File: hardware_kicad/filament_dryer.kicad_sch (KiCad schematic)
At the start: 140 parts, among them J1 USB_C_Receptacle_USB2.0, J2 H/T Ambient, J3 T Aux, J4 Peristaltic Pump, Q3 NMOS, Q4 NMOS, Q5 NMOS, Q6 NMOS, Q7 NMOS, Q8 NMOS, U1 W25Q128JVS, U2 AMS1117-3.3, U3 RP2040, U4 DS18B20Z, U5 H/T Filament, X1 12MHz Yangxing Tech X322512MS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

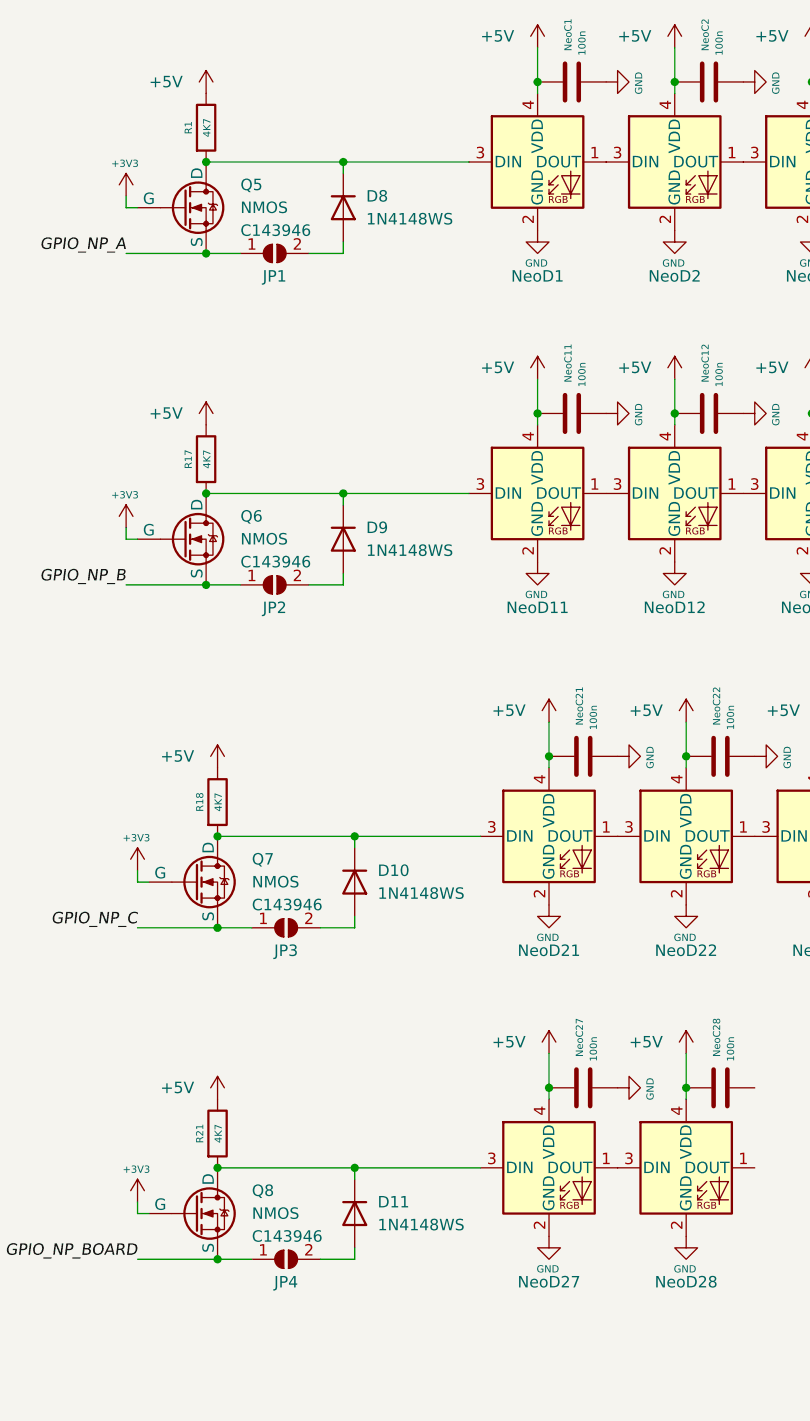
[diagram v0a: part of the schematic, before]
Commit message: Remove 4 diodes
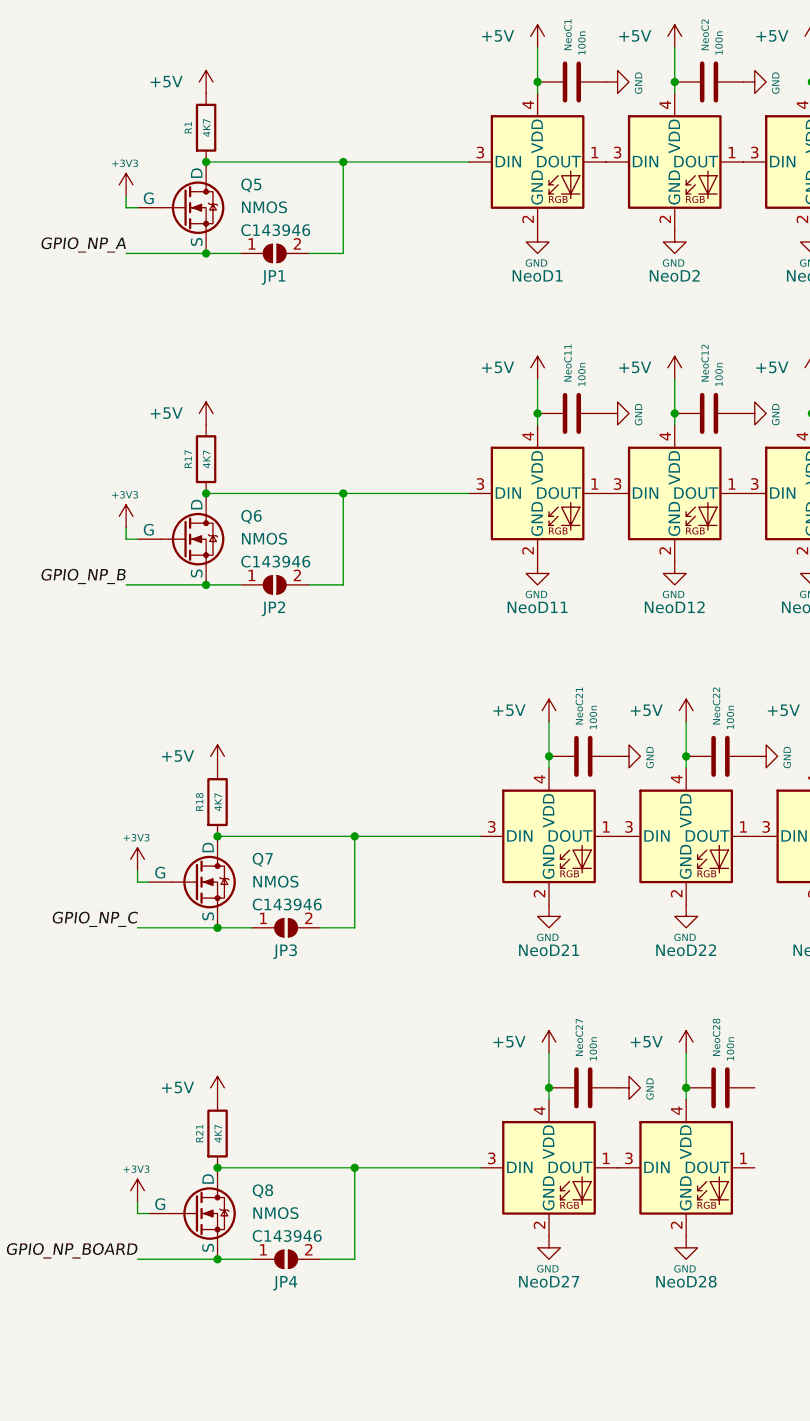
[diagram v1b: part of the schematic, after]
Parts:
- removed D10, D11, D8, D9: 1N4148WS, Diode_SMD:D_SOD-323, symbol Diode:1N4148WS
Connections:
- net at NeoD27.3 (DIN), Q8.1 (D), R21.2: now also JP4.2 (B)
- net at NeoD11.3 (DIN), Q6.1 (D), R17.2: now also JP2.2 (B)
- net at JP1.2 (B): now also NeoD1.3 (DIN), Q5.1 (D), R1.2
- net at NeoD21.3 (DIN), Q7.1 (D), R18.2: now also JP3.2 (B)
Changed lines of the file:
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@@
     (stroke (width 0) (type solid))
   )
-  (wire (pts (xy 167.64 510.54) (xy 167.64 511.81))
-    (stroke (width 0) (type default))
-  )
   (wire (pts (xy 85.09 33.02) (xy 90.17 33.02))
     (stroke (width 0) (type solid))
@@
     (stroke (width 0) (type default))
   )
-  (wire (pts (xy 166.37 408.94) (xy 166.37 407.67))
-    (stroke (width 0) (type default))
-  )
   (wire (pts (xy 279.4 422.91) (xy 279.4 426.72))
     (stroke (width 0) (type default))
@@
     (stroke (width 0) (type default))
   )
-  (wire (pts (xy 167.64 520.7) (xy 167.64 519.43))
-    (stroke (width 0) (type default))
-  )
   (wire (pts (xy 320.04 44.45) (xy 320.04 45.72))
     (stroke (width 0) (type solid))
@@
     (stroke (width 0) (type default))
   )
-  (wire (pts (xy 167.64 473.71) (xy 167.64 474.98))
-    (stroke (width 0) (type default))
-  )
   (wire (pts (xy 140.97 181.61) (xy 140.97 182.88))
     (stroke (width 0) (type default))
@@
     (stroke (width 0) (type default))
   )
+  (wire (pts (xy 167.64 510.54) (xy 167.64 520.7))
+    (stroke (width 0) (type default))
+  )
   (wire (pts (xy 269.24 255.27) (xy 273.05 255.27))
     (stroke (width 0) (type default))
@@
     (stroke (width 0) (type default))
   )
-  (wire (pts (xy 166.37 398.78) (xy 166.37 400.05))
+  (wire (pts (xy 166.37 398.78) (xy 166.37 408.94))
     (stroke (width 0) (type default))
   )
@@
     (stroke (width 0) (type default))
   )
-  (wire (pts (xy 166.37 445.77) (xy 166.37 444.5))
-    (stroke (width 0) (type default))
-  )
   (polyline (pts (xy 204.47 146.05) (xy 163.83 146.05))
     (stroke (width 0) (type default))
@@
     (stroke (width 0) (type solid))
   )
-  (wire (pts (xy 166.37 435.61) (xy 166.37 436.88))
+  (wire (pts (xy 166.37 435.61) (xy 166.37 445.77))
     (stroke (width 0) (type default))
   )
@@
     (stroke (width 0) (type solid))
   )
-  (wire (pts (xy 167.64 483.87) (xy 167.64 482.6))
+  (wire (pts (xy 167.64 473.71) (xy 167.64 483.87))
     (stroke (width 0) (type default))
   )
@@
     )
   )
-  (symbol (lib_id "Diode:1N4148WS") (at 166.37 403.86 270) (unit 1)
-    (in_bom yes) (on_board yes) (dnp no) (fields_autoplaced)
-    (property "Reference" "D8" (at 168.91 402.59 90)
-      (effects (font (size 1.27 1.27)) (justify left))
-    )
-    (property "Value" "1N4148WS" (at 168.91 405.13 90)
-      (effects (font (size 1.27 1.27)) (justify left))
-    )
-    (property "Footprint" "Diode_SMD:D_SOD-323" (at 161.925 403.86 0)
-      (effects (font (size 1.27 1.27)) hide)
-    )
-    (property "Datasheet" "https://www.vishay.com/docs/85751/1n4148ws.pdf" (at 166.37 403.86 0)
-      (effects (font (size 1.27 1.27)) hide)
-    )
-    (property "Sim.Device" "D" (at 166.37 403.86 0)
-      (effects (font (size 1.27 1.27)) hide)
-    )
-    (property "Sim.Pins" "1=K 2=A" (at 166.37 403.86 0)
-      (effects (font (size 1.27 1.27)) hide)
-    )
-    (property "JLC Part" "C417545" (at 166.37 403.86 0)
-      (effects (font (size 1.27 1.27)) hide)
-    )
-    (pin "1")
-    (pin "2")
-    (instances
-      (project "filament_dryer"
-        (path "/35c47459-45a7-4753-acae-c8b47e7575e1"
-          (reference "D8") (unit 1)
-        )
-      )
-    )
-  )
   (symbol (lib_id "power:+3V3") (at 102.87 30.48 0) (unit 1)
     (in_bom yes) (on_board yes) (dnp no)
@@
     )
   )
-  (symbol (lib_id "Diode:1N4148WS") (at 167.64 515.62 270) (unit 1)
-    (in_bom yes) (on_board yes) (dnp no) (fields_autoplaced)
-    (property "Reference" "D11" (at 170.18 514.35 90)
-      (effects (font (size 1.27 1.27)) (justify left))
-    )
-    (property "Value" "1N4148WS" (at 170.18 516.89 90)
-      (effects (font (size 1.27 1.27)) (justify left))
-    )
-    (property "Footprint" "Diode_SMD:D_SOD-323" (at 163.195 515.62 0)
-      (effects (font (size 1.27 1.27)) hide)
-    )
-    (property "Datasheet" "https://www.vishay.com/docs/85751/1n4148ws.pdf" (at 167.64 515.62 0)
-      (effects (font (size 1.27 1.27)) hide)
-    )
-    (property "Sim.Device" "D" (at 167.64 515.62 0)
-      (effects (font (size 1.27 1.27)) hide)
-    )
-    (property "Sim.Pins" "1=K 2=A" (at 167.64 515.62 0)
-      (effects (font (size 1.27 1.27)) hide)
-    )
-    (property "JLC Part" "C417545" (at 167.64 515.62 0)
-      (effects (font (size 1.27 1.27)) hide)
-    )
-    (pin "1")
-    (pin "2")
-    (instances
-      (project "filament_dryer"
-        (path "/35c47459-45a7-4753-acae-c8b47e7575e1"
-          (reference "D11") (unit 1)
-        )
-      )
-    )
-  )
   (symbol (lib_id "power:GND") (at 257.81 464.82 90) (unit 1)
     (in_bom yes) (on_board yes) (dnp no)
@@
     )
   )
-  (symbol (lib_id "Diode:1N4148WS") (at 166.37 440.69 270) (unit 1)
-    (in_bom yes) (on_board yes) (dnp no) (fields_autoplaced)
-    (property "Reference" "D9" (at 168.91 439.42 90)
-      (effects (font (size 1.27 1.27)) (justify left))
-    )
-    (property "Value" "1N4148WS" (at 168.91 441.96 90)
-      (effects (font (size 1.27 1.27)) (justify left))
-    )
-    (property "Footprint" "Diode_SMD:D_SOD-323" (at 161.925 440.69 0)
-      (effects (font (size 1.27 1.27)) hide)
-    )
-    (property "Datasheet" "https://www.vishay.com/docs/85751/1n4148ws.pdf" (at 166.37 440.69 0)
-      (effects (font (size 1.27 1.27)) hide)
-    )
-    (property "Sim.Device" "D" (at 166.37 440.69 0)
-      (effects (font (size 1.27 1.27)) hide)
-    )
-    (property "Sim.Pins" "1=K 2=A" (at 166.37 440.69 0)
-      (effects (font (size 1.27 1.27)) hide)
-    )
-    (property "JLC Part" "C417545" (at 166.37 440.69 0)
-      (effects (font (size 1.27 1.27)) hide)
-    )
-    (pin "1")
-    (pin "2")
-    (instances
-      (project "filament_dryer"
-        (path "/35c47459-45a7-4753-acae-c8b47e7575e1"
-          (reference "D9") (unit 1)
-        )
-      )
-    )
-  )
   (symbol (lib_id "power:+5V") (at 264.16 422.91 0) (unit 1)
     (in_bom yes) (on_board yes) (dnp no)
@@
         )
       )
-    )
-  )
-  (symbol (lib_id "Diode:1N4148WS") (at 167.64 478.79 270) (unit 1)
-    (in_bom yes) (on_board yes) (dnp no) (fields_autoplaced)
-    (property "Reference" "D10" (at 170.18 477.52 90)
-      (effects (font (size 1.27 1.27)) (justify left))
-    )
-    (property "Value" "1N4148WS" (at 170.18 480.06 90)
-      (effects (font (size 1.27 1.27)) (justify left))
-    )
-    (property "Footprint" "Diode_SMD:D_SOD-323" (at 163.195 478.79 0)
-      (effects (font (size 1.27 1.27)) hide)
-    )
-    (property "Datasheet" "https://www.vishay.com/docs/85751/1n4148ws.pdf" (at 167.64 478.79 0)
-      (effects (font (size 1.27 1.27)) hide)
-    )
-    (property "Sim.Device" "D" (at 167.64 478.79 0)
-      (effects (font (size 1.27 1.27)) hide)
-    )
-    (property "Sim.Pins" "1=K 2=A" (at 167.64 478.79 0)
-      (effects (font (size 1.27 1.27)) hide)
-    )
-    (property "JLC Part" "C417545" (at 167.64 478.79 0)
-      (effects (font (size 1.27 1.27)) hide)
-    )
-    (pin "1")
-    (pin "2")
-    (instances
-      (project "filament_dryer"
-        (path "/35c47459-45a7-4753-acae-c8b47e7575e1"
-          (reference "D10") (unit 1)
-        )
-      )

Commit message: After second review
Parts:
- removed D4, D5: 1N4148WS, Diode_SMD:D_SOD-323, symbol Diode:1N4148WS
- added D1, D2: General Purpose Diode, Diode_SMD:D_SMA, symbol 00_project_library:GeneralPurposeDiode
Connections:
- net GPIO_HEATER_1 is gone; now on net HT_GROVE_SCL: U3.16 (GPIO13)
- net GPIO_HEATER_2 is gone; now on net T_AUX_1WIRE: U3.17 (GPIO14)
- net +5V: now also D1.1 (K), D2.1 (K)
- net GND: now also NeoC28.2
- net GPIO_FAN_SILICAGEL: now also U3.12 (GPIO9)
- net HT_GROVE_SCL: no longer U3.14 (GPIO11), U3.7 (GPIO5)
- net HT_GROVE_SDA: now also U3.15 (GPIO12); no longer U3.13 (GPIO10), U3.6 (GPIO4)
- net T_AUX_1WIRE: no longer U3.15 (GPIO12)
- net at Q4.1 (D), TP10.1: now also D2.2 (A)
- net at Q3.1 (D), TP8.1: now also D1.2 (A)
- no-connect marks 19 -> 28

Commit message: After second review 2
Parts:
- D3, D6, D7: footprint LED_SMD:LED_0603_1608Metric -> 00_project_library:LED_0603_1608Metric
- NeoD1, NeoD10, NeoD11, NeoD12, NeoD13, NeoD14, NeoD15, NeoD16, NeoD17, NeoD18, NeoD19, NeoD2, NeoD20, NeoD21, NeoD22, NeoD23, NeoD24, NeoD25, NeoD26, NeoD27, NeoD28, NeoD3, NeoD4, NeoD5, NeoD6, NeoD7, NeoD8, NeoD9: footprint LED_SMD:LED_WS2812B-2020_PLCC4_2.0x2.0mm -> 00_project_library:LED_WS2812B-2020_PLCC4_2.0x2.0mm
- Q3, Q4, Q5, Q6, Q7, Q8: footprint Package_TO_SOT_SMD:SOT-23 -> 00_project_library:SOT-23
- U1: footprint Package_SO:SOIC-8_5.23x5.23mm_P1.27mm -> 00_project_library:SOIC-8_5.23x5.23mm_P1.27mm
- U4: footprint Package_SO:SOIC-8_3.9x4.9mm_P1.27mm -> 00_project_library:SOIC-8_3.9x4.9mm_P1.27mm
- X1: footprint Crystal:Crystal_SMD_3225-4Pin_3.2x2.5mm -> 00_project_library:Crystal_SMD_3225-4Pin_3.2x2.5mm

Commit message: hardware_kicad v0.6
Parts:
- D1, D2: footprint Diode_SMD:D_SMA -> 00_project_library:D_SMA
- NeoD1, NeoD10, NeoD11, NeoD12, NeoD13, NeoD14, NeoD15, NeoD16, NeoD17, NeoD18, NeoD19, NeoD2, NeoD20, NeoD21, NeoD22, NeoD23, NeoD24, NeoD25, NeoD26, NeoD27, NeoD28, NeoD3, NeoD4, NeoD5, NeoD6, NeoD7, NeoD8, NeoD9: footprint 00_project_library:LED_WS2812B-2020_PLCC4_2.0x2.0mm -> LED_SMD:LED_WS2812B-2020_PLCC4_2.0x2.0mm
- U2: footprint Package_TO_SOT_SMD:SOT-223-3_TabPin2 -> 00_project_library:SOT-223-3_TabPin2

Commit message: tmp
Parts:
- removed C1, C10, C11, C12, C2, C3, C6, C7, C8, C9, NeoC1, NeoC10, NeoC11, NeoC12, NeoC13, NeoC14, NeoC15, NeoC16, NeoC17, NeoC18, NeoC19, NeoC2, NeoC20, NeoC21, NeoC22, NeoC23, NeoC24, NeoC25, NeoC26, NeoC27, NeoC28, NeoC3, NeoC4, NeoC5, NeoC6, NeoC7, NeoC8, NeoC9: 100n, Capacitor_SMD:C_0402_1005Metric_Pad0.74x0.62mm_HandSolder, symbol 00_project_library:C
- removed C13, C15: 10u, Capacitor_SMD:C_0603_1608Metric, symbol 00_project_library:C
- removed C17, C18: 30p, Capacitor_SMD:C_0402_1005Metric, symbol 00_project_library:C
- removed C4, C5: 1u, Capacitor_SMD:C_0402_1005Metric_Pad0.74x0.62mm_HandSolder, symbol 00_project_library:C
- removed D3: POW_LED, 00_project_library:LED_0603_1608Metric, symbol 00_project_library:LED
- removed J1: USB_C_Receptacle_USB2.0, 00_project_library:USB_C_Receptacle_Palconn_UTC16-G, symbol 00_project_library:USB_C_Receptacle_USB2.0
- removed JP1, JP2, JP3, JP4: SolderJumper_2_Open, Jumper:SolderJumper-2_P1.3mm_Open_RoundedPad1.0x1.5mm, symbol Jumper:SolderJumper_2_Open
- removed NeoD1, NeoD10, NeoD11, NeoD12, NeoD13, NeoD14, NeoD15, NeoD16, NeoD17, NeoD18, NeoD19, NeoD2, NeoD20, NeoD21, NeoD22, NeoD23, NeoD24, NeoD25, NeoD26, NeoD27, NeoD28, NeoD3, NeoD4, NeoD5, NeoD6, NeoD7, NeoD8, NeoD9: WS2812B-2020, LED_SMD:LED_WS2812B-2020_PLCC4_2.0x2.0mm, symbol 00_project_library:WS2812B-2020
- removed Q5, Q6, Q7, Q8: NMOS, 00_project_library:SOT-23, symbol 00_project_library:NMOS
- removed R10: 1k, Resistor_SMD:R_0402_1005Metric_Pad0.72x0.64mm_HandSolder, symbol 00_project_library:R
- removed R17, R18, R21: 4K7, Resistor_SMD:R_0402_1005Metric_Pad0.72x0.64mm_HandSolder, symbol 00_project_library:R
- removed R2, R9: 10K, Resistor_SMD:R_0402_1005Metric_Pad0.72x0.64mm_HandSolder, symbol 00_project_library:R
- removed R3, R4: 5.1K, Resistor_SMD:R_0402_1005Metric_Pad0.72x0.64mm_HandSolder, symbol 00_project_library:R_Small
- removed R5, R6: 27R, Resistor_SMD:R_0402_1005Metric_Pad0.72x0.64mm_HandSolder, symbol 00_project_library:R
- removed R8: 470R, Resistor_SMD:R_0402_1005Metric_Pad0.72x0.64mm_HandSolder, symbol 00_project_library:R
- removed SW_BOOT1: Boot, 00_project_library:SW_TS-1187A-B-A-B, symbol 00_project_library:SW_MEC_5E
- removed SW_RESET1: Reset, 00_project_library:SW_TS-1187A-B-A-B, symbol 00_project_library:SW_MEC_5E
- removed TP1: TestPoint, TestPoint:TestPoint_Pad_D2.5mm, symbol Connector:TestPoint
- removed U1: W25Q128JVS, 00_project_library:SOIC-8_5.23x5.23mm_P1.27mm, symbol 00_project_library:W25Q128JVS
- removed U2: AMS1117-3.3, 00_project_library:SOT-223-3_TabPin2, symbol Regulator_Linear:AMS1117-3.3
- removed U3: RP2040, 00_project_library_circuitstate:RP2040-QFN-56, symbol 00_project_library:RP2040
- removed X1: 12MHz Yangxing Tech X322512MSB4SI, 00_project_library:Crystal_SMD_3225-4Pin_3.2x2.5mm, symbol 00_project_library:Crystal_GND24_Small
- added U1: Pico, RPi_Pico:RPi_Pico_SMD_TH, symbol 00_project_library:Pico
- R1: value 4K7 -> R; footprint Resistor_SMD:R_0402_1005Metric_Pad0.72x0.64mm_HandSolder -> (none)
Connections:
- net +5V: no longer R1.1
- no-connect marks 28 -> 3
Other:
- note added: "Heater Resistors"
- note removed: "Bypass Capacitors"
- note removed: "C1, C2 = 2*CL - 2*Cs CL = 20pF, Cs can be ~5pF"
- note removed: "Crystal"
- note removed: "Flash Memory"
- note removed: "Main Regulator"
- note removed: "Make sure 27R are close to RP2040"
- note removed: "Neopixel WS2812B-2020"
- note removed: "Place 1uF close to pin 44"
- note removed: "Place 1uF close to pin 45"
- note removed: "Power LED"
- note removed: "RP2040"
- note removed: "Reset"
- note removed: "USB Type-C"

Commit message: schematics
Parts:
- added D3: Power_LED_1, 00_project_library:LED_0603_1608Metric, symbol 00_project_library:LED
- added D4: Power_LED_2, 00_project_library:LED_0603_1608Metric, symbol 00_project_library:LED
- added PowerQ1, PowerQ2: NMOS, 00_project_library:SOT-23, symbol 00_project_library:NMOS
- added PowerR1, PowerR10, PowerR11, PowerR12, PowerR13, PowerR14, PowerR15, PowerR16, PowerR17, PowerR18, PowerR19, PowerR2, PowerR20, PowerR21, PowerR22, PowerR23, PowerR24, PowerR3, PowerR4, PowerR5, PowerR6, PowerR7, PowerR8, PowerR9: 120, Resistor_SMD:R_1206_3216Metric, symbol 00_project_library:R_POWER
- added R2: 470R, Resistor_SMD:R_0402_1005Metric_Pad0.72x0.64mm_HandSolder, symbol 00_project_library:R
- R1: value R -> 470R; footprint (none) -> Resistor_SMD:R_0402_1005Metric_Pad0.72x0.64mm_HandSolder
- U1: footprint RPi_Pico:RPi_Pico_SMD_TH -> 00_project_library:RPi_Pico_SMD_TH
- renumbered Q3 to FanQ1, Q4 to FanQ2
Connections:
- net +5V: now also D3.2 (A), D4.2 (A), PowerR1.1, PowerR10.1, PowerR11.1, PowerR12.1, PowerR13.1, PowerR14.1, PowerR15.1, PowerR16.1, PowerR17.1, PowerR18.1, PowerR19.1, PowerR2.1, PowerR20.1, PowerR21.1, PowerR22.1, PowerR23.1, PowerR24.1, PowerR3.1, PowerR4.1, PowerR5.1, PowerR6.1, PowerR7.1, PowerR8.1, PowerR9.1
- net GND: now also PowerQ1.3 (S), PowerQ2.3 (S)
- net at R1.1: now also D4.1 (K)
- net at R1.2: now also PowerQ2.1 (D), PowerR13.2, PowerR14.2, PowerR15.2, PowerR16.2, PowerR17.2, PowerR18.2, PowerR19.2, PowerR20.2, PowerR21.2, PowerR22.2, PowerR23.2, PowerR24.2
- new net: PowerQ1.1 (D), PowerR1.2, PowerR10.2, PowerR11.2, PowerR12.2, PowerR2.2, PowerR3.2, PowerR4.2, PowerR5.2, PowerR6.2, PowerR7.2, PowerR8.2, PowerR9.2, R2.2
- new net: D3.1 (K), R2.1
- new net GPIO_HEATER: PowerQ1.2 (G), PowerQ2.2 (G)

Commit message: schematics ready for review
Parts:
- removed J2: H/T Ambient, 00_project_library:grove_vert_holes, symbol 00_project_library:grove_vert_holes_1
- removed J3: T Aux, 00_project_library:grove_vert_holes, symbol 00_project_library:grove_vert_holes
- removed R13, R14: 10k, Resistor_SMD:R_0402_1005Metric_Pad0.72x0.64mm_HandSolder, symbol 00_project_library:R
- removed R16: 4k7, Resistor_SMD:R_0402_1005Metric_Pad0.72x0.64mm_HandSolder, symbol 00_project_library:R
- added C1, C2: 10u, Capacitor_SMD:C_0603_1608Metric, symbol 00_project_library:C
- added R3, R4, R5, R6, R7, R8: 10k, Resistor_SMD:R_0402_1005Metric_Pad0.72x0.64mm_HandSolder, symbol 00_project_library:R
- added U2, U3: H/T Filament, 00_project_library:SON50P250X250X90-9T110X180N, symbol 00_project_library:SHT31-DIS
- H1, H2, H3, H4, H5: footprint MountingHole:MountingHole_3.2mm_M3 -> 00_project_library:MountingHole_3.2mm_M3
- R15: value 4k7 -> 2k
- TP11: value HT_SILICAGEL_SCL -> HT_AMBIENT_SCL
- TP2: value HT_SILICAGEL_GND -> HT_AMBIENT_GND
- TP3: value HT_SILICAGEL_3V3 -> HT_AMBIENT_3V3
- TP6: value HT_SILICAGEL_SCA -> HT_AMBIENT_SCA
- U5: value H/T Filament -> H/T Silicagel
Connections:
- net +3V3: now also U1.36 (3V3), C1.1, C2.1, R3.1, R4.1, R5.1, R6.1, R7.1, R8.1, U2.2 (ADDR), U2.5 (VDD), U3.2 (ADDR), U3.5 (VDD); no longer R12.1
- net +5V: now also U1.40 (VBUS)
- net GND: now also R12.2, U1.13 (GND), U1.18 (GND), U1.23 (GND), U1.28 (GND), U1.3 (GND), U1.38 (GND), U1.8 (GND), C1.2, C2.2, U2.7 (R), U2.8 (VSS), U2.9 (VSS), U3.7 (R), U3.8 (VSS), U3.9 (VSS)
- net at U5.6 (~{RESET}): now also R12.1; no longer R12.2
- net GPIO_HEATER renamed GPIO_HEATER_A
- net GPIO_HEATER_A: no longer PowerQ2.2 (G)
- net HT_BOARD_SCL renamed HT_AMBIENT_SCL
- net HT_AMBIENT_SCL: now also R8.2, U3.4 (SCL); no longer U5.4 (SCL)
- net HT_BOARD_SDA renamed HT_AMBIENT_SDA
- net HT_AMBIENT_SDA: now also R7.2, U3.1 (SDA); no longer U5.1 (SDA)
- new net: R3.2, U2.6 (~{RESET})
- new net: R6.2, U3.6 (~{RESET})
- new net GPIO_HEATER_B: PowerQ2.2 (G)
- new net HT_FILAMENT_SCL: R5.2, U2.4 (SCL), U5.4 (SCL)
- new net HT_FILAMENT_SDA: R4.2, U2.1 (SDA), U5.1 (SDA)
- no-connect marks 3 -> 4
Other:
- note added: "H/T Ambient I2C0 0x45"
- note added: "H/T Ambient spare I2C0 0x45"
- note removed: "H/T Ambient I2C0 0x44"
- moved on the sheet: C14, C20, R12, R15, U4, U5
